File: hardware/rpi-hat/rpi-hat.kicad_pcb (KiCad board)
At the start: 2 copper layers, 65 x 56 mm, 28 parts, among them J1 Conn_02x20_Odd_Even__Rpi, J10 Conn_01x02_Male

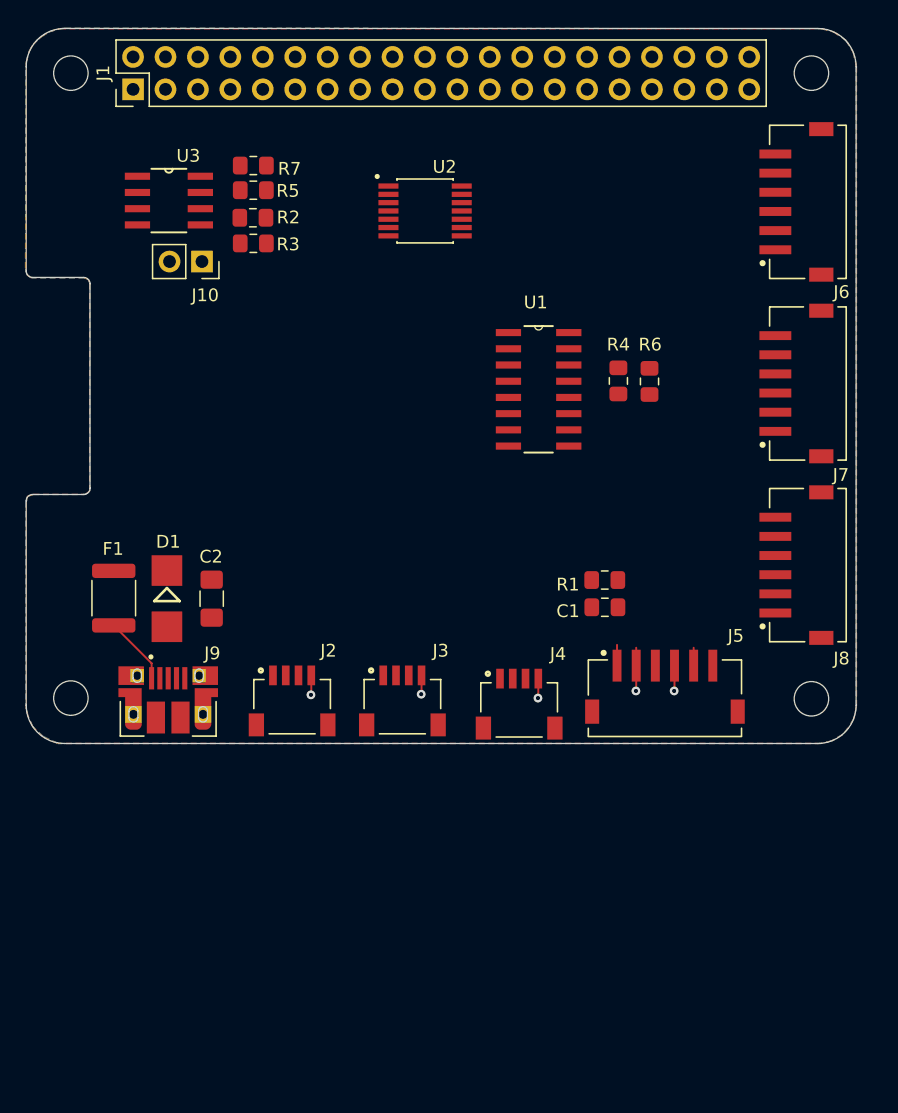
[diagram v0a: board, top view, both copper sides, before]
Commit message: New HAT features.
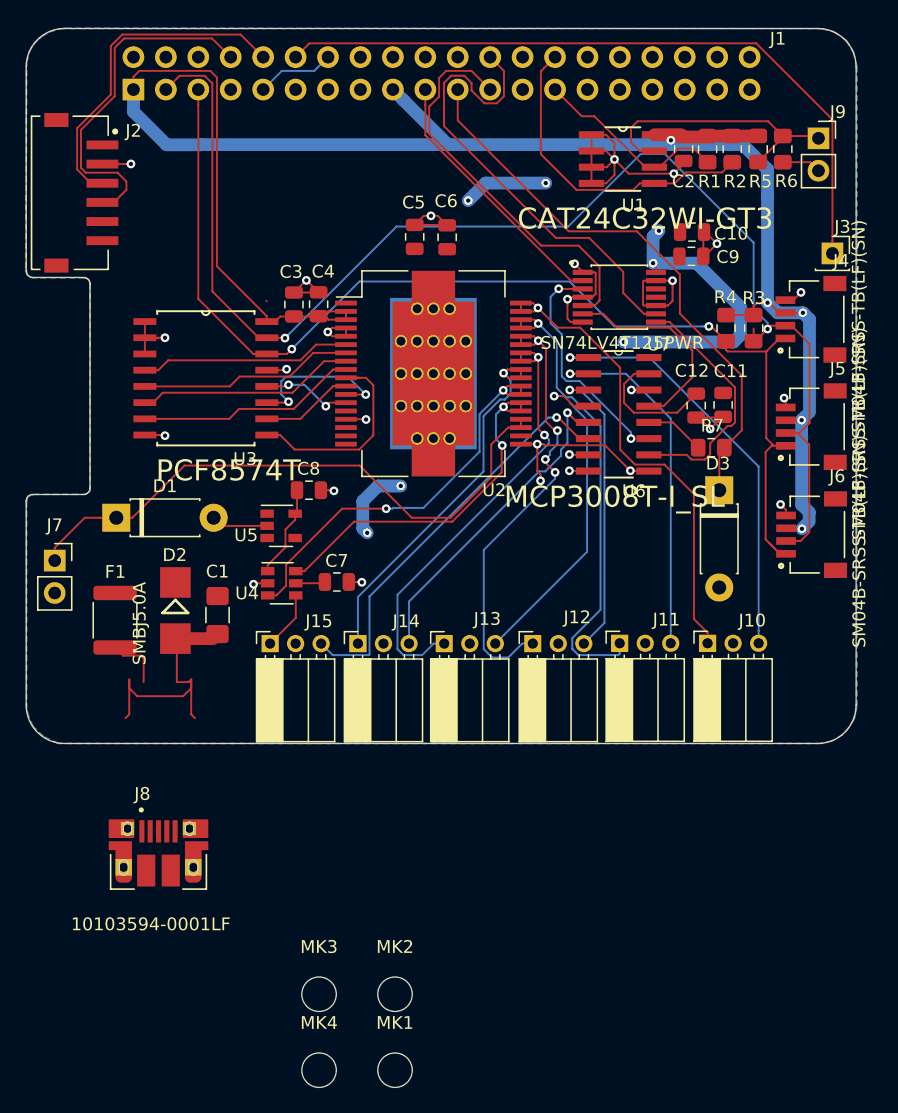
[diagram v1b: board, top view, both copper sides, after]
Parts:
- removed ? (x4): M2.5, MountingHole:MountingHole_2.7mm_M2.5
- added C10: 10uF, Capacitor_SMD:C_0805_2012Metric, F.Cu at (252.1, 109.9)
- added C11: 10uF, Capacitor_SMD:C_0805_2012Metric, F.Cu at (254.6, 123.5)
- added C12: 100nF, Capacitor_SMD:C_0805_2012Metric, F.Cu at (252.5, 123.5)
- added C3: 100nF, Capacitor_SMD:C_0805_2012Metric, F.Cu at (221.0, 115.6)
- added C4: 100nF, Capacitor_SMD:C_0805_2012Metric, F.Cu at (222.9, 115.6)
- added C5: 100nF, Capacitor_SMD:C_0805_2012Metric, F.Cu at (230.4, 110.3)
- added C6: 47uF, Capacitor_SMD:C_0805_2012Metric, F.Cu at (233.0, 110.4)
- added C7: 1uF, Capacitor_SMD:C_0805_2012Metric, F.Cu at (224.3, 137.4)
- added C8: 1uF, Capacitor_SMD:C_0805_2012Metric, F.Cu at (222.1, 130.2)
- added C9: 100nF, Capacitor_SMD:C_0805_2012Metric, F.Cu at (252.1, 111.8)
- added D2: SMBJ5.0A, zephyrus-iaq:SMBJ5.0A, F.Cu at (211.7, 139.6)
- added D3: 1N4728A_3.3V_100uA, Diode_THT:D_DO-41_SOD81_P7.62mm_Horizontal, F.Cu at (254.3, 130.2)
- added J11: Conn_MQ_Gas, Connector_PinSocket_2.00mm:PinSocket_1x03_P2.00mm_Horizontal, F.Cu at (246.5, 142.2)
- added J12: Conn_MQ_Gas, Connector_PinSocket_2.00mm:PinSocket_1x03_P2.00mm_Horizontal, F.Cu at (239.7, 142.2)
- added J13: Conn_MQ_Gas, Connector_PinSocket_2.00mm:PinSocket_1x03_P2.00mm_Horizontal, F.Cu at (232.7, 142.2)
- added J14: Conn_MQ_Gas, Connector_PinSocket_2.00mm:PinSocket_1x03_P2.00mm_Horizontal, F.Cu at (226.0, 142.2)
- added J15: Conn_MQ_Gas, Connector_PinSocket_2.00mm:PinSocket_1x03_P2.00mm_Horizontal, F.Cu at (219.1, 142.2)
- added MK1: M2.5, MountingHole:MountingHole_2.7mm_M2.5, F.Cu at (228.9, 175.6)
- added MK2: M2.5, MountingHole:MountingHole_2.7mm_M2.5, F.Cu at (228.9, 169.6)
- added MK3: M2.5, MountingHole:MountingHole_2.7mm_M2.5, F.Cu at (222.9, 169.6)
- added MK4: M2.5, MountingHole:MountingHole_2.7mm_M2.5, F.Cu at (222.9, 175.6)
- added U4: SN74LVC1G3157, Package_TO_SOT_SMD:SOT-23-6, F.Cu at (220.0, 137.5)
- added U5: NCP699, Package_TO_SOT_SMD:SOT-23-5, F.Cu at (220.0, 133.0)
- added U6: MCP3008T-I_SL, MCP3008T-I_SL:SOIC127P600X175-16N, F.Cu at (246.4, 124.2)
- added U7: SN74LV4T125PWR, SN74LV4T125PWR:SOP65P640X120-14N, F.Cu at (246.5, 115.0)
- C1: value 220uF -> 47uF; footprint Resistor_SMD:R_0805_2012Metric_Pad1.15x1.40mm_HandSolder -> Resistor_SMD:R_1206_3216Metric_Pad1.42x1.75mm_HandSolder
- C2: value 47uF -> 100nF; footprint Resistor_SMD:R_1206_3216Metric_Pad1.42x1.75mm_HandSolder -> Capacitor_SMD:C_0805_2012Metric
- D1: value (none) -> D_Zener; footprint zephyrus-iaq:SMBJ5.0A -> Diode_THT:D_DO-41_SOD81_P7.62mm_Horizontal
- J1: footprint Connector_PinHeader_2.54mm:PinHeader_2x20_P2.54mm_Vertical -> Connector_PinSocket_2.54mm:PinSocket_2x20_P2.54mm_Vertical; moved to B.Cu
- J10: value Conn_01x02_Male -> Conn_MQ_Gas; footprint Connector_PinSocket_2.54mm:PinSocket_1x02_P2.54mm_Vertical -> Connector_PinSocket_2.00mm:PinSocket_1x03_P2.00mm_Horizontal
- J2: footprint SM04B-SRSS-TB_LF__SN_:JST_SM04B-SRSS-TB(LF)(SN) -> S6B-ZR-SM4A-TF_LF__SN_:JST_S6B-ZR-SM4A-TF(LF)(SN)
- J3: value (none) -> Conn_01x01_Female; footprint SM04B-SRSS-TB_LF__SN_:JST_SM04B-SRSS-TB(LF)(SN) -> Connector_PinSocket_2.54mm:PinSocket_1x01_P2.54mm_Vertical
- J4: value (none) -> SM04B-SRSS-TB(LF)(SN)
- J5, J6: value (none) -> SM04B-SRSS-TB(LF)(SN); footprint S6B-ZR-SM4A-TF_LF__SN_:JST_S6B-ZR-SM4A-TF(LF)(SN) -> SM04B-SRSS-TB_LF__SN_:JST_SM04B-SRSS-TB(LF)(SN)
- J7: value (none) -> Conn_01x02_Female; footprint S6B-ZR-SM4A-TF_LF__SN_:JST_S6B-ZR-SM4A-TF(LF)(SN) -> Connector_PinSocket_2.54mm:PinSocket_1x02_P2.54mm_Vertical
- J8: value (none) -> 10103594-0001LF; footprint S6B-ZR-SM4A-TF_LF__SN_:JST_S6B-ZR-SM4A-TF(LF)(SN) -> 10103594-0001LF:FCI_10103594-0001LF
- J9: value (none) -> Conn_01x02_Male; footprint 10103594-0001LF:FCI_10103594-0001LF -> Connector_PinSocket_2.54mm:PinSocket_1x02_P2.54mm_Vertical
- R1: value 150 -> 3.9k
- R3: value 3.9k -> 10k
- R4: value 1700 -> 10k
- R6: value 3300 -> DNP
- R7: value DNP -> 270
- U1: value (none) -> CAT24C32WI-GT3; footprint MCP3008T-I_SL:SOIC127P600X175-16N -> CAT24C32WI-GT3:SOIC127P600X175-8N
- U2: value (none) -> ISO1H811G; footprint SN74LV4T125PWR:SOP65P640X120-14N -> Package_SO:HSOP-36-1EP_11.0x15.9mm_P0.65mm_SlugDown_ThermalVias
- U3: value (none) -> PCF8574T; footprint CAT24C32WI-GT3:SOIC127P600X175-8N -> zephyrus-iaq:SOIC127P1032X265-16N
- moved J9 68.0 mm to (262.1, 102.6)
- moved J7 58.1 mm to (202.2, 135.7), turned to 0 degrees
- moved J8 53.8 mm to (210.4, 159.7), turned to 0 degrees
- moved C2 51.1 mm to (251.5, 103.4)
- moved J10 49.6 mm to (253.4, 142.2), turned to 90 degrees
- moved J3 47.2 mm to (263.1, 111.6)
- moved R7 42.1 mm to (253.7, 126.8), turned to 0 degrees
- moved J2 40.6 mm to (206.0, 106.9), turned to 270 degrees
- moved R3 39.7 mm to (257.0, 117.5), turned to 270 degrees
- moved R5 39.7 mm to (257.3, 103.4), turned to 270 degrees
- moved R2 37.9 mm to (255.3, 103.5), turned to 270 degrees
- moved J4 35.0 mm to (259.5, 116.8), turned to 90 degrees
- moved R1 34.7 mm to (253.4, 103.5), turned to 270 degrees
- moved C1 30.3 mm to (215.0, 139.9), turned to 270 degrees
- moved J6 26.1 mm to (259.5, 133.6)
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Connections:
- C1 pad 1: Net-(C1-Pad1) -> +5V
- C2 pad 1: +5V -> +3V3
- D1 pad 1: +5V -> /Vfan
- J1 pad 10: /GPIO15(RXD0) -> RXD0
- J1 pad 11: ADC0_En -> /GPIO17(GEN0)
- J1 pad 12: PWM0_3.3 -> GPS_PPS
- J1 pad 13: ADC1_En -> /GPIO27(GEN2)
- J1 pad 15: ADC2_En -> /GPIO22(GEN3)
- J1 pad 19: MOSI_3.3 -> /GPIO10(SPI0_MOSI)
- J1 pad 21: MISO_3.3 -> /GPIO9(SPI0_MISO)
- J1 pad 23: SCK_3.3 -> /GPIO11(SPI0_SCK)
- J1 pad 24: ~CE~_3.3 -> /GPIO8(SPI0_CE_N)
- J1 pad 28: ID_SC_EEPROM -> /ID_SC_EEPROM
- J1 pad 29: ADC3_En -> /GPIO5
- J1 pad 31: ADC4_En -> /GPIO6
- J1 pad 37: ADC5_En -> /GPIO26
- J1 pad 8: /GPIO14(TXD0) -> TXD0
- J10 pad 1: Net-(J10-Pad1) -> /Analog_Sensors/Vswitch0
- J2 pad 1: SCL -> +5V
- J2 pad 2: SDA -> GND
- J2 pad 3: +3V3 -> RXD0
- J2 pad 4: GND -> TXD0
- J3 pad 1: SCL -> GPS_PPS
- J5 pad 1: Net-(C1-Pad1) -> SCL
- J5 pad 2: GND -> SDA
- J5 pad 3: PWM0_5 -> +3V3
- J6 pad 1: +5V -> SCL
- J6 pad 2: ADC1 -> SDA
- J6 pad 3: ADC0 -> +3V3
- J6 pad 4: ADC0_En -> GND
- J7 pad 1: +5V -> /Vfan
- J7 pad 2: ADC3 -> GND
- J8 pad 1: +5V -> Net-(F1-Pad2)
- J8 pad 2: ADC5 -> Net-(J8-Pad2)
- J8 pad 3: ADC4 -> Net-(J8-Pad3)
- J8 pad 4: ADC4_En -> Net-(J8-Pad4)
- J8 pad 5: ADC5_En -> GND
- J9 pad 1: Net-(F1-Pad2) -> Net-(J9-Pad1)
- J9 pad 2: Net-(J9-Pad2) -> GND
- R1 pad 1: Net-(C1-Pad1) -> +3V3
- R1 pad 2: +5V -> ID_SD_EEPROM
- R2 pad 2: ID_SD_EEPROM -> /ID_SC_EEPROM
- R3 pad 2: ID_SC_EEPROM -> SDA
- R4 pad 1: Net-(R4-Pad1) -> +3V3
- R4 pad 2: MISO_3.3 -> SCL
- R5 pad 2: Net-(J10-Pad1) -> Net-(J9-Pad1)
- R6 pad 1: MISO_3.3 -> GND
- R6 pad 2: GND -> Net-(J9-Pad1)
- R7 pad 1: GND -> Net-(R7-Pad1)
- R7 pad 2: Net-(J10-Pad1) -> /GPIO9(SPI0_MISO)
- U1 pad 1: ADC0 -> GND
- U1 pad 2: ADC1 -> GND
- U1 pad 3: ADC2 -> GND
- U1 pad 4: ADC3 -> GND
- U1 pad 5: ADC4 -> /ID_SC_EEPROM
- U1 pad 6: ADC5 -> ID_SD_EEPROM
- U1 pad 7: ADC6 -> Net-(J9-Pad1)
- U1 pad 8: Net-(U1-Pad8) -> +3V3
- U2 pad 1: GND -> Net-(U2-Pad1)
- U2 pad 10: GND -> /Analog_Sensors/D4
- U2 pad 11: PWM0_5 -> /Analog_Sensors/D5
- U2 pad 12: PWM0_3.3 -> /Analog_Sensors/D6
- U2 pad 13: GND -> /Analog_Sensors/D7
- U2 pad 14: +5V -> Net-(U2-Pad14)
- U2 pad 2: SCK_3.3 -> +3V3
- U2 pad 3: SCK_5 -> +3V3
- U2 pad 5: MOSI_3.3 -> GND
- U2 pad 6: MOSI_5 -> /Analog_Sensors/D0
- U2 pad 7: GND -> /Analog_Sensors/D1
- U2 pad 8: ~CE~_5 -> /Analog_Sensors/D2
- U2 pad 9: ~CE~_3.3 -> /Analog_Sensors/D3
- U3 pad 4: GND -> /Analog_Sensors/D0
- U3 pad 5: ID_SC_EEPROM -> /Analog_Sensors/D1
- U3 pad 6: ID_SD_EEPROM -> /Analog_Sensors/D2
- U3 pad 7: Net-(J10-Pad1) -> /Analog_Sensors/D3
- U3 pad 8: +3V3 -> GND
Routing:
- net +3V3: track 0.00 -> 150.1 mm, vias 0 -> 5
- net GND: track 9.94 -> 129.6 mm, vias 5 -> 25
- net SDA: track 0.00 -> 107.2 mm, vias 0 -> 2
- net SCL: track 0.00 -> 89.2 mm, vias 0 -> 2
- net +5V: track 0.00 -> 55.6 mm, vias 0 -> 7
- net GPS_PPS: track 0.00 -> 55.5 mm
- net /Vfan: track 0.00 -> 47.0 mm
- net /GPIO9(SPI0_MISO): track 0.00 -> 44.5 mm
- net /Analog_Sensors/Vswitch0: track 0.00 -> 37.7 mm, vias 0 -> 1
- net /Analog_Sensors/Vswitch1: track 0.00 -> 37.1 mm, vias 0 -> 1
- net /GPIO8(SPI0_CE_N): track 0.00 -> 36.9 mm
- net /Analog_Sensors/Vswitch2: track 0.00 -> 36.2 mm, vias 0 -> 4
- net /Analog_Sensors/Vswitch3: track 0.00 -> 36.0 mm, vias 0 -> 2
- net /ADC0: track 0.00 -> 33.6 mm, vias 0 -> 1
- net /ADC5: track 0.00 -> 32.4 mm, vias 0 -> 1
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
